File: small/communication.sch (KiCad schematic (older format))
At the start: 14 parts, among them J5 Conn_02x04_Odd_Even, U14 ST485EBDR, U9 ISO1540

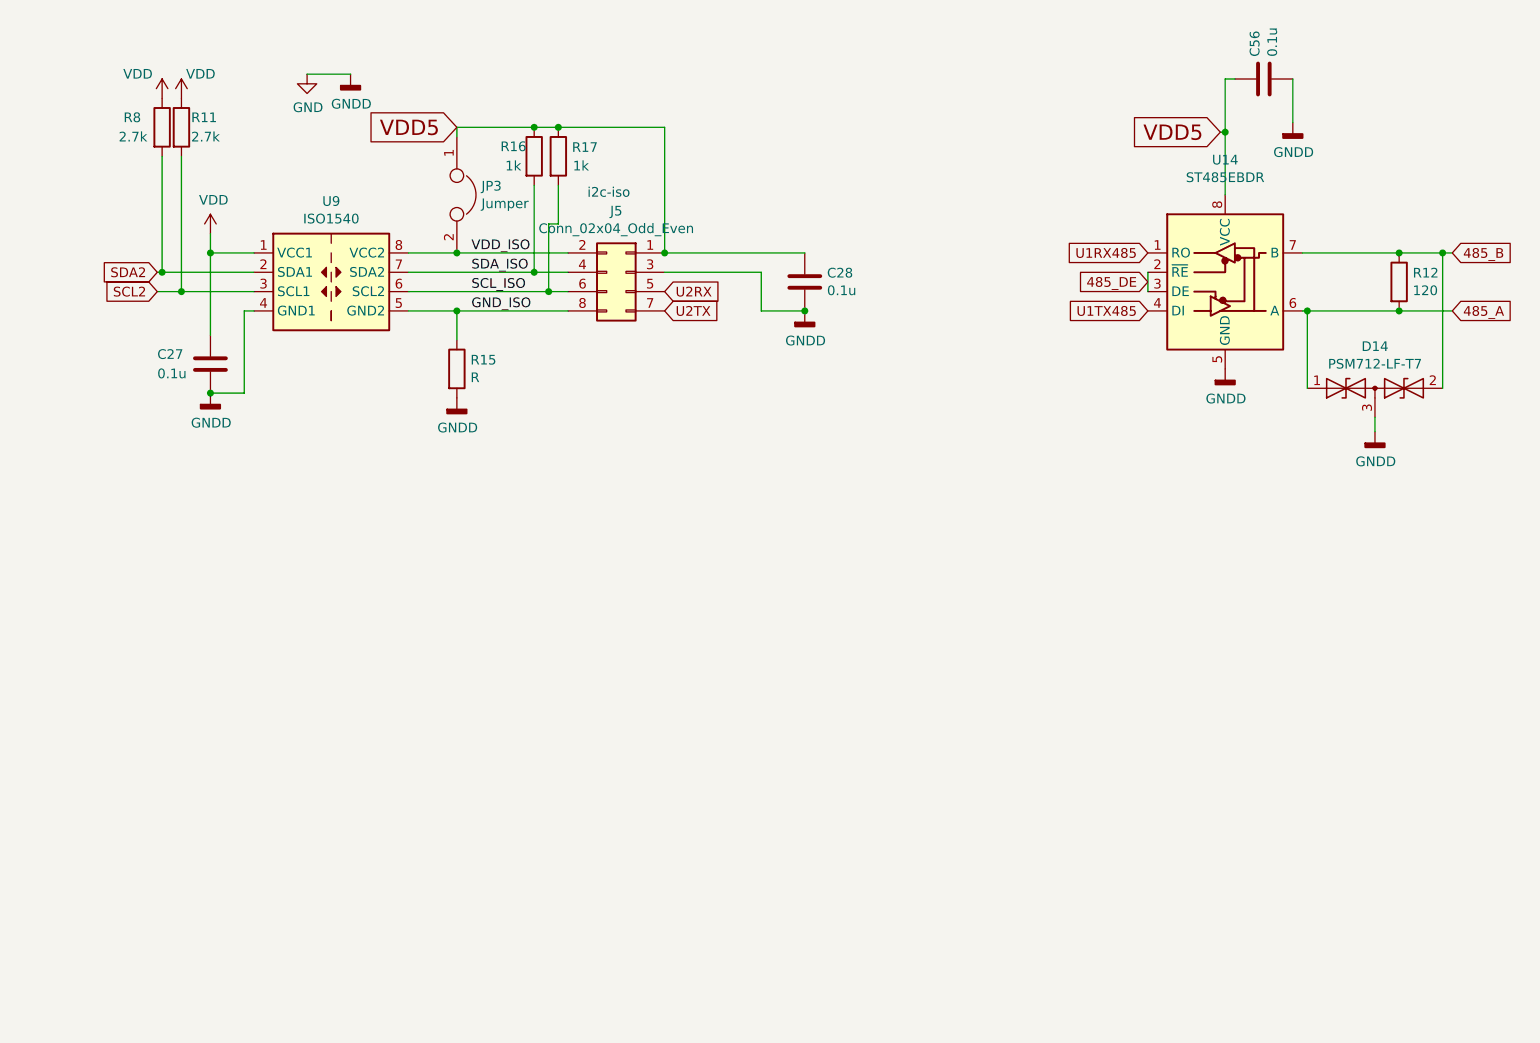
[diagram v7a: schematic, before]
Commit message: Isolated DCDC added
power LED added
reverse voltage protection added
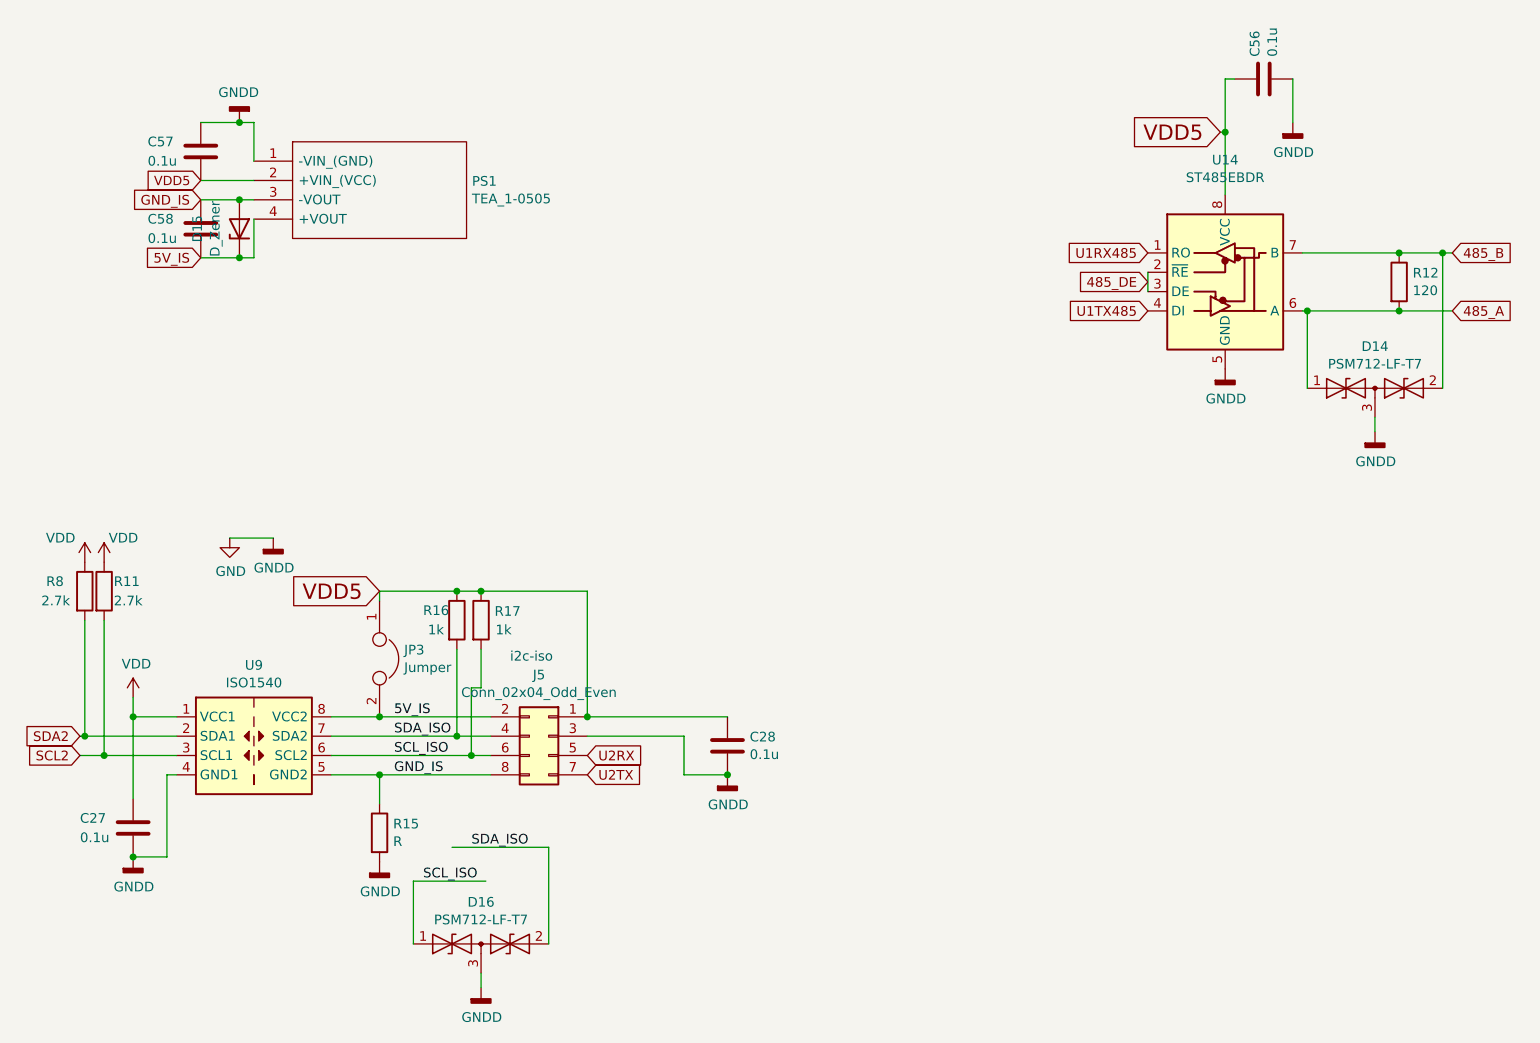
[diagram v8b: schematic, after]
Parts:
- added C57, C58: 0.1u, Capacitor_SMD:C_0603_1608Metric, symbol Device:C
- added D15: D_Zener, Diode_SMD:D_MiniMELF, symbol Device:D_Zener
- added D16: PSM712-LF-T7, Package_TO_SOT_SMD:SOT-23, symbol Diode:SM712_SOT23
- added PS1: TEA_1-0505, small:TEA10505, symbol TEA_1-0505:TEA_1-0505
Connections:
- net labels added: 5V_IS, GND_IS
- net labels removed: GND_ISO, VDD_ISO
- wire segments 50 -> 64
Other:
- moved on the sheet: C27, C28, J5, JP3, R11, R15, R16, R17, R8, U9
